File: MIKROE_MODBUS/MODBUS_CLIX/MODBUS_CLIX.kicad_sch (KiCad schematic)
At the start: 39 parts, among them J1 Conn_01x02_Pin, J10 Conn_01x02_Pin, J11 Conn_01x03_Pin, J12 Conn_01x02_Pin, J2 Conn_01x02_Pin, J3 Conn_01x02_Pin, J4 Conn_01x02_Pin, J5 Conn_01x02_Pin, J6 Conn_01x02_Pin, J7 TERMINAL BLOCK, J8 Conn_01x02_Pin, J9 Conn_01x02_Pin, U1 CLICK BOARD, U2 MAX485E, U3 MT3608

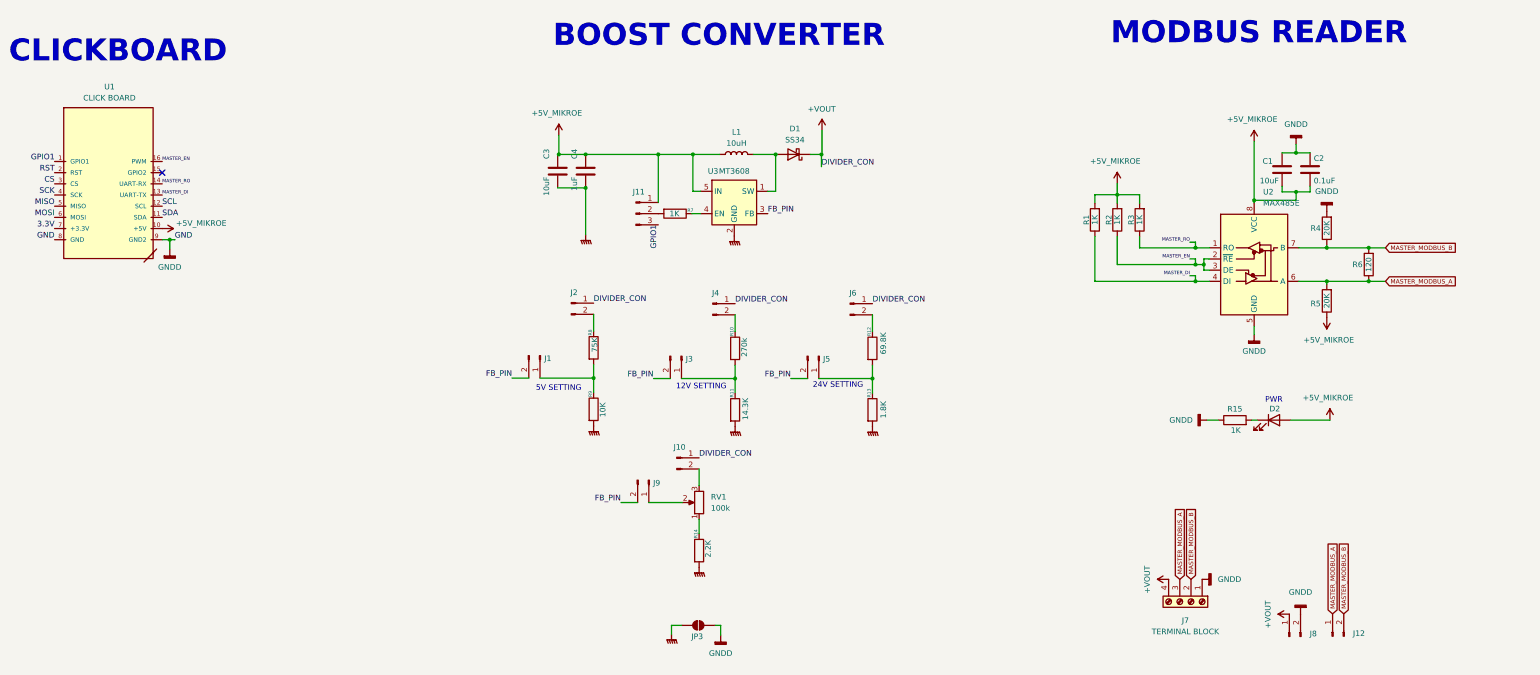
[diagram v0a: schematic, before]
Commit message: Updated Schematic
Simplified Jumper Settings
remove 5V out option from MT3608
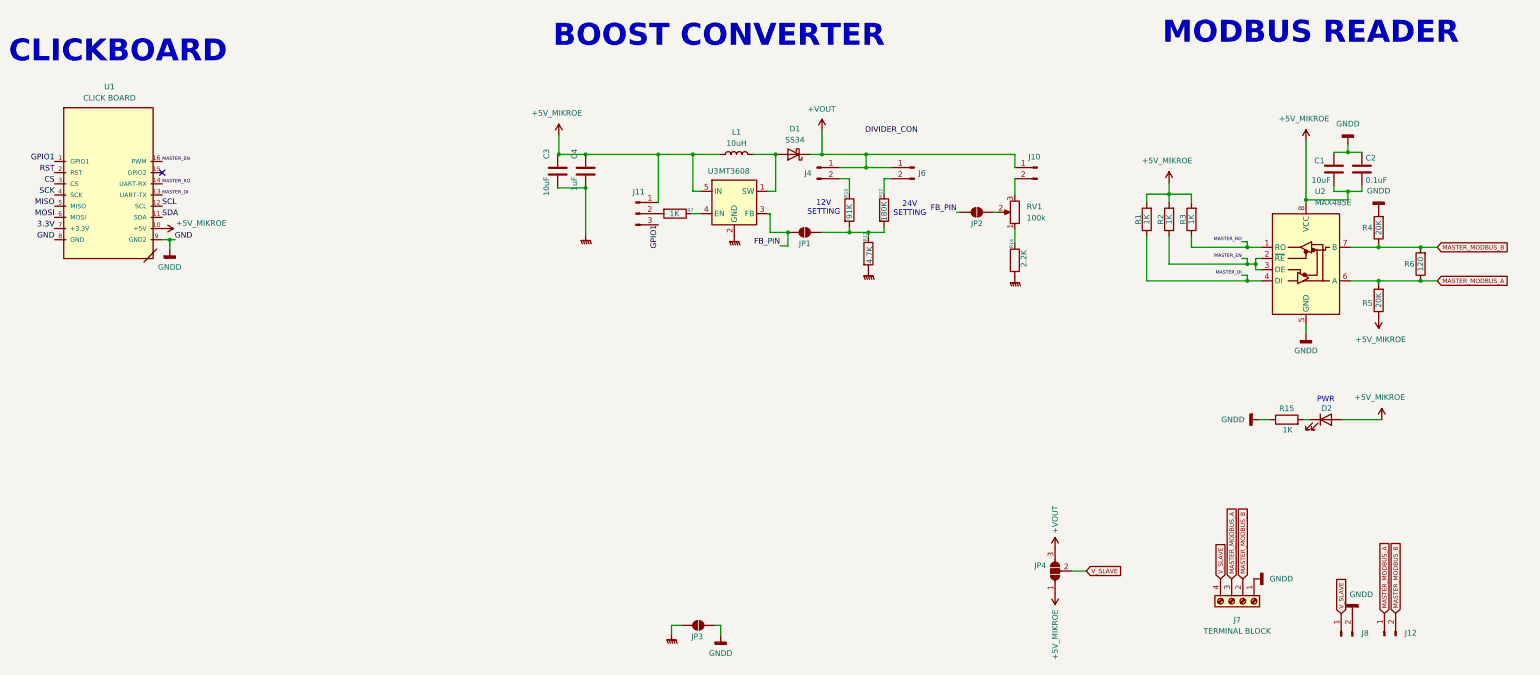
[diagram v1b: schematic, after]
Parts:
- removed J1, J2, J3, J5, J9: Conn_01x02_Pin, Connector_PinHeader_2.54mm:PinHeader_1x02_P2.54mm_Vertical, symbol Connector:Conn_01x02_Pin
- removed R11: 14.3K, Resistor_SMD:R_0603_1608Metric_Pad0.98x0.95mm_HandSolder, symbol Device:R
- removed R8: 75K, Resistor_SMD:R_0603_1608Metric_Pad0.98x0.95mm_HandSolder, symbol Device:R
- removed R9: 10K, Resistor_SMD:R_0603_1608Metric_Pad0.98x0.95mm_HandSolder, symbol Device:R
- added JP1, JP2: SolderJumper_2_Open, symbol Jumper:SolderJumper_2_Open
- added JP4: SolderJumper_3_Open, symbol Jumper:SolderJumper_3_Open
- R10: value 270k -> 91K
- R12: value 69.8K -> 180K
- R13: value 1.8K -> 4.7K
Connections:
- net +5V_MIKROE: now also JP4.1 (A)
- net +VOUT: now also JP4.3 (B); no longer J7.4 (Pin_4), J8.1 (Pin_1)
- net FB_PIN: now also JP1.1 (A), JP2.1 (A)
- net at R10.2: now also R12.2, R13.1, JP1.2 (B)
- net at RV1.2: now also JP2.2 (B)
- new net V_SLAVE: J7.4 (Pin_4), J8.1 (Pin_1), JP4.2 (C)
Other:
- note removed: "5V SETTING"
- moved on the sheet: C1, C2, D2, J10, J12, J4, J6, J7, J8, R1, R10, R12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

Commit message: -
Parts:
- JP1, JP2: footprint (none) -> Jumper:SolderJumper-2_P1.3mm_Open_Pad1.0x1.5mm
- JP4: footprint (none) -> Jumper:SolderJumper-3_P1.3mm_Open_Pad1.0x1.5mm
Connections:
- net GNDD: now also J7.4 (Pin_4); no longer J7.1 (Pin_1)
- net MASTER_MODBUS_A: now also J7.2 (Pin_2); no longer J7.3 (Pin_3)
- net MASTER_MODBUS_B: now also J7.3 (Pin_3); no longer J7.2 (Pin_2)
- net V_SLAVE: now also J7.1 (Pin_1); no longer J7.4 (Pin_4)
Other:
- moved on the sheet: J7
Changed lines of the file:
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@@
 		)
 	)
-	(label "DIVIDER_CON"
-		(at 250.952 78.994 0)
+	(label "SCK"
+		(at 66.7535 92.853 180)
 		(fields_autoplaced yes)
 		(effects
@@
 				(size 1.27 1.27)
 			)
+			(justify right bottom)
+		)
+	)
+	(label "MASTER_EN"
+		(at 91.2137 85.233 0)
+		(fields_autoplaced yes)
+		(effects
+			(font
+				(size 0.762 0.762)
+			)
 			(justify left bottom)
 		)
 	)
-	(label "SCK"
-		(at 66.7535 92.853 180)
+	(label "CS"
+		(at 66.7535 90.313 180)
 		(fields_autoplaced yes)
 		(effects
@@
 		)
 	)
-	(label "MASTER_EN"
-		(at 91.2137 85.233 0)
-		(fields_autoplaced yes)
-		(effects
-			(font
-				(size 0.762 0.762)
-			)
-			(justify left bottom)
-		)
-	)
-	(label "CS"
-		(at 66.7535 90.313 180)
+	(label "GND"
+		(at 66.7535 103.013 180)
 		(fields_autoplaced yes)
 		(effects
@@
 		)
 	)
-	(label "GND"
-		(at 66.7535 103.013 180)
+	(label "GPIO1"
+		(at 66.7535 85.233 180)
 		(fields_autoplaced yes)
 		(effects
@@
 		)
 	)
-	(label "GPIO1"
-		(at 66.7535 85.233 180)
-		(fields_autoplaced yes)
-		(effects
-			(font
-				(size 1.27 1.27)
-			)
-			(justify right bottom)
-		)
-	)
 	(global_label "MASTER_MODBUS_A"
 		(shape input)
@@
 			)
 		)
-		(property "Footprint" ""
+		(property "Footprint" "Jumper:SolderJumper-2_P1.3mm_Open_Pad1.0x1.5mm"
 			(at 276.352 96.774 0)
 			(effects
@@
 			)
 		)
-		(property "Footprint" ""
+		(property "Footprint" "Jumper:SolderJumper-2_P1.3mm_Open_Pad1.0x1.5mm"
 			(at 237.236 101.346 0)
 			(effects
@@
 			)
 		)
-		(property "Footprint" ""
+		(property "Footprint" "Jumper:SolderJumper-3_P1.3mm_Open_Pad1.0x1.5mm"
 			(at 294.132 178.308 0)
 			(effects
@@
 	(symbol
 		(lib_id "Connector:Screw_Terminal_01x04")
-		(at 336.804 185.166 270)
-		(unit 1)
-		(exclude_from_sim no)
-		(in_bom yes)
-		(on_board yes)
-		(dnp no)
-		(fields_autoplaced yes)
+		(at 334.264 185.166 90)
+		(mirror x)
+		(unit 1)
+		(exclude_from_sim no)
+		(in_bom yes)
+		(on_board yes)
+		(dnp no)
 		(property "Reference" "J7"
 			(at 335.534 189.4321 90)
@@
 		)
 		(property "Footprint" "TerminalBlock:TerminalBlock_Xinya_XY308-2.54-4P_1x04_P2.54mm_Horizontal"
-			(at 336.804 185.166 0)
+			(at 334.264 185.166 0)
 			(effects
 				(font
@@
 		)
 		(property "Datasheet" "~"
-			(at 336.804 185.166 0)
+			(at 334.264 185.166 0)
 			(effects
 				(font
@@
 		)
 		(property "Description" "Generic screw terminal, single row, 01x04, script generated (kicad-library-utils/schlib/autogen/connector/)"
-			(at 336.804 185.166 0)
-			(effects
-				(font
+			(at 334.264 185.166 0)
+			(effects
+				(font

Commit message: Initial Design Review
1. Set unused MikroE pins to Unconnected
2. Edited Silk Screen details
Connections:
- net 3.3V: no longer names the net of U1.7 (+3.3V)
- net CS: no longer names the net of U1.3 (CS)
- net MISO: no longer names the net of U1.5 (MISO)
- net MOSI: no longer names the net of U1.6 (MOSI)
- net RST: no longer names the net of U1.2 (RST)
- net SCK: no longer names the net of U1.4 (SCK)
- net SCL: no longer names the net of U1.12 (SCL)
- net SDA: no longer names the net of U1.11 (SDA)
- no-connect marks 1 -> 9
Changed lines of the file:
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@@
+	)
+	(no_connect
+		(at 66.7535 87.773)
+	)
+	(no_connect
+		(at 66.7535 95.393)
 	)
 	(no_connect
 		(at 91.2137 87.773)
+	)
+	(no_connect
+		(at 91.2137 95.393)
+	)
+	(no_connect
+		(at 66.7535 100.473)
+	)
+	(no_connect
+		(at 66.7535 97.933)
+	)
+	(no_connect
+		(at 66.7535 90.313)
+	)
+	(no_connect
+		(at 91.2137 97.933)
+	)
+	(no_connect
+		(at 66.7535 92.853)
 	)
 	(wire
@@
 		)
 	)
-	(label "SDA"
-		(at 91.2137 97.933 0)
-		(fields_autoplaced yes)
-		(effects
-			(font
-				(size 1.27 1.27)
-			)
-			(justify left bottom)
-		)
-	)
 	(label "FB_PIN"
 		(at 231.648 104.394 180)
@@
 		)
 	)
-	(label "3.3V"
-		(at 66.7535 100.473 180)
-		(fields_autoplaced yes)
-		(effects
-			(font
-				(size 1.27 1.27)
-			)
-			(justify right bottom)
-		)
-	)
-	(label "MISO"
-		(at 66.7535 95.393 180)
-		(fields_autoplaced yes)
-		(effects
-			(font
-				(size 1.27 1.27)
-			)
-			(justify right bottom)
-		)
-	)
-	(label "RST"
-		(at 66.7535 87.773 180)
-		(fields_autoplaced yes)
-		(effects
-			(font
-				(size 1.27 1.27)
-			)
-			(justify right bottom)
-		)
-	)
 	(label "MASTER_RO"
 		(at 91.2137 90.313 0)
@@
 		)
 	)
-	(label "SCL"
-		(at 91.2137 95.393 0)
-		(fields_autoplaced yes)
-		(effects
-			(font
-				(size 1.27 1.27)
-			)
-			(justify left bottom)
-		)
-	)
 	(label "GND"
 		(at 94.0624 103.0251 0)
@@
 		)
 	)
-	(label "MOSI"
-		(at 66.7535 97.933 180)
-		(fields_autoplaced yes)
-		(effects
-			(font
-				(size 1.27 1.27)
-			)
-			(justify right bottom)
-		)
-	)
-	(label "SCK"
-		(at 66.7535 92.853 180)
-		(fields_autoplaced yes)
-		(effects
-			(font
-				(size 1.27 1.27)
-			)
-			(justify right bottom)
-		)
-	)
 	(label "MASTER_EN"
 		(at 91.2137 85.233 0)
@@
 		)
 	)
-	(label "CS"
-		(at 66.7535 90.313 180)
-		(fields_autoplaced yes)
-		(effects
-			(font
-				(size 1.27 1.27)
-			)
-			(justify right bottom)
-		)
-	)

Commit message: -
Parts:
- added JP5: SolderJumper_2_Open, Jumper:SolderJumper-2_P1.3mm_Open_Pad1.0x1.5mm, symbol Jumper:SolderJumper_2_Open
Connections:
- net MASTER_MODBUS_B: now also JP5.2 (B); no longer R6.2
- new net: JP5.1 (A), R6.2
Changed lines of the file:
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@@
 	)
 	(junction
+		(at 367.6719 104.7367)
+		(diameter 0)
+		(color 0 0 0 0)
+	)
+	(junction
 		(at 367.6719 112.3567)
 		(diameter 0)
@@
 	)
 	(junction
-		(at 367.6719 104.7367)
+		(at 377.1969 94.4121)
 		(diameter 0)
 		(color 0 0 0 0)
@@
 		(color 0 0 0 0)
 	)
-	(junction
-		(at 377.1969 104.7367)
-		(diameter 0)
-		(color 0 0 0 0)
-	)
 	(no_connect
 		(at 66.7535 87.773)
@@
 	(wire
 		(pts
-			(xy 377.1969 104.7367) (xy 381.0069 104.7367)
-		)
-		(stroke
-			(width 0)
-			(type default)
-		)
-	)
-	(wire
-		(pts
 			(xy 187.4433 83.6256) (xy 203.9533 83.6256)
 		)
@@
 	(wire
 		(pts
+			(xy 377.1969 94.4121) (xy 372.1588 94.4121)
+		)
+		(stroke
+			(width 0)
+			(type default)
+		)
+	)
+	(wire
+		(pts
 			(xy 363.8619 92.0367) (xy 363.8619 90.7667)
 		)
@@
 	(wire
 		(pts
-			(xy 325.1269 102.1967) (xy 325.1269 104.7367)
+			(xy 372.1588 94.4121) (xy 372.1588 104.7367)
 		)
 		(stroke
@@
 	(wire
 		(pts
-			(xy 229.362 101.346) (xy 233.426 101.346)
+			(xy 325.1269 102.1967) (xy 325.1269 104.7367)
 		)
 		(stroke
@@
 	(wire
 		(pts
-			(xy 367.6719 104.7367) (xy 377.1969 104.7367)
+			(xy 229.362 101.346) (xy 233.426 101.346)
 		)
 		(stroke
@@
 	(wire
 		(pts
+			(xy 377.1969 94.4121) (xy 383.9418 94.4121)
+		)
+		(stroke
+			(width 0)
+			(type default)
+		)
+	)
+	(wire
+		(pts
 			(xy 357.5119 90.7667) (xy 357.5119 92.0367)
 		)
@@
 	(wire
 		(pts
+			(xy 377.1969 94.4121) (xy 377.1969 97.1167)
+		)
+		(stroke
+			(width 0)
+			(type default)
+		)
+	)
+	(wire
+		(pts
 			(xy 284.988 86.614) (xy 284.988 83.6256)
 		)
@@
 	(wire
 		(pts
+			(xy 372.1588 104.7367) (xy 367.6719 104.7367)
+		)
+		(stroke
+			(width 0)
+			(type default)
+		)
+	)
+	(wire
+		(pts
 			(xy 211.8273 83.6256) (xy 211.8273 92.0076)
 		)
@@
 	(global_label "MASTER_MODBUS_B"
 		(shape input)
-		(at 381.0069 104.7367 0)
+		(at 383.9418 94.4121 0)
 		(fields_autoplaced yes)
 		(effects
@@
 		)
 		(property "Intersheetrefs" "${INTERSHEET_REFS}"
-			(at 397.6906 104.7367 0)
+			(at 400.6255 94.4121 0)
 			(effects
 				(font
@@
 					(unit 1)
 				)
+			)
+		)
+	)
+	(symbol
+		(lib_id "Jumper:SolderJumper_2_Open")
+		(at 377.1969 100.9267 90)
+		(unit 1)
+		(exclude_from_sim yes)
+		(in_bom no)
+		(on_board yes)
+		(dnp no)
+		(property "Reference" "JP5"
+			(at 379.7369 100.9267 0)
+			(effects
+				(font
+					(size 1.27 1.27)
+				)
+			)
+		)
+		(property "Value" "SolderJumper_2_Open"
+			(at 373.6409 100.9267 0)
+			(effects
+				(font
+					(size 1.27 1.27)
+				)
+				(hide yes)
+			)
+		)
+		(property "Footprint" "Jumper:SolderJumper-2_P1.3mm_Open_Pad1.0x1.5mm"
+			(at 377.1969 100.9267 0)
+			(effects
+				(font
+					(size 1.27 1.27)
+				)
+				(hide yes)
+			)
+		)
+		(property "Datasheet" "~"
+			(at 377.1969 100.9267 0)
+			(effects
+				(font
+					(size 1.27 1.27)
+				)
+				(hide yes)
+			)
+		)
+		(property "Description" "Solder Jumper, 2-pole, open"
+			(at 377.1969 100.9267 0)
+			(effects
+				(font
+					(size 1.27 1.27)
+				)
+				(hide yes)
+			)
+		)
+		(pin "1"
+		)
+		(pin "2"
+		)
+		(instances
+			(project "MODBUS_CLIX"
+				(path "/9261da16-fb7d-40d7-ab0d-e30fadb62d03"
+					(reference "JP5")
+					(unit 1)
+				)

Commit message: -
panelization
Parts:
- U1: footprint MIKROE:MIKROE-PINS -> MIKROE_3800:MIKROE-3800
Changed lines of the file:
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@@
 			)
 		)
-		(property "Footprint" "MIKROE:MIKROE-PINS"
+		(property "Footprint" "MIKROE_3800:MIKROE-3800"
 			(at 79.4535 95.393 0)
 			(effects
